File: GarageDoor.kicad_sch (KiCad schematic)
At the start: 30 parts, among them J1 1935161.0, J2 EB21A-04-C, J3 EB21A-04-C, K1 SRD-12VDC-SL-C, K2 SRD-12VDC-SL-C, Q1 BS170-D26Z, Q2 BS170-D26Z, Q3 IRFR9024NTRLPBF, U1 LM2596, U2 WeMos_D1_mini

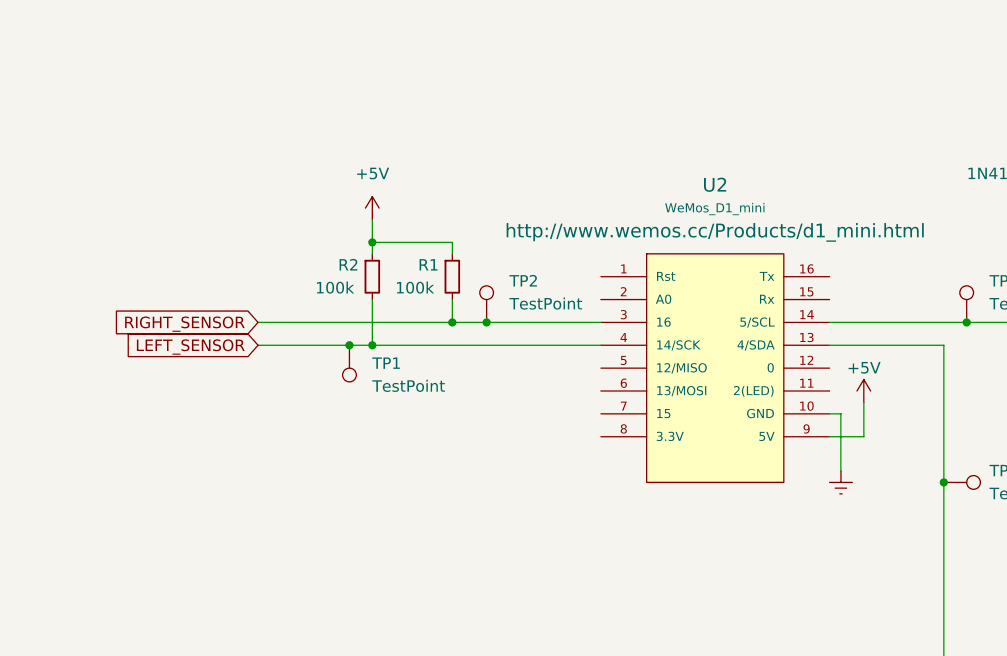
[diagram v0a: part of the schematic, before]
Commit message: Connect unused pins to ground.
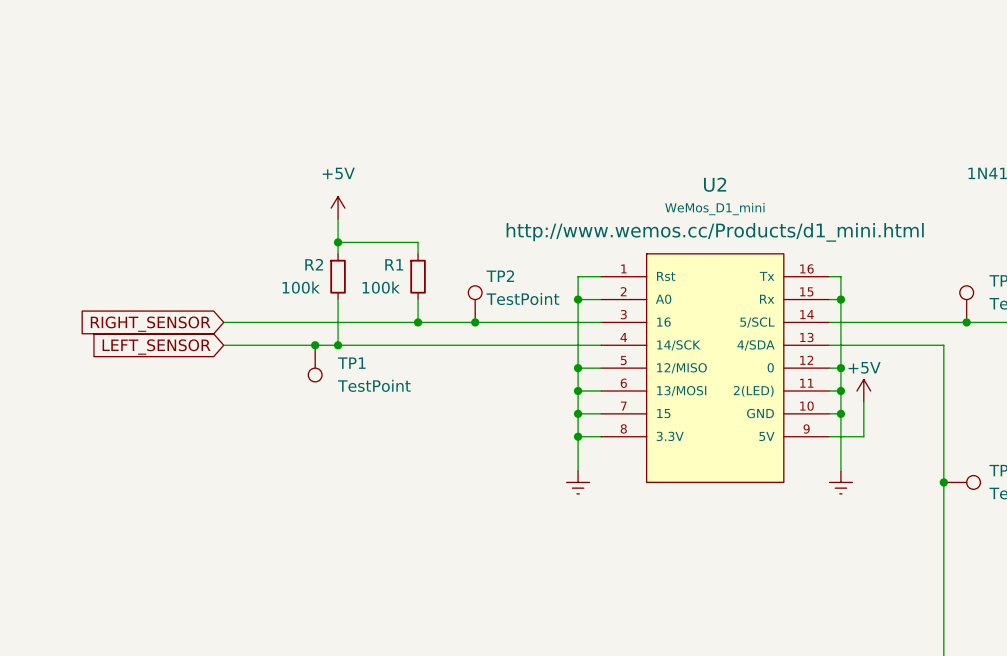
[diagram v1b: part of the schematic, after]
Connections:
- net Earth: now also U2.1 (Rst), U2.11 (2(LED)), U2.12 (0), U2.15 (Rx), U2.16 (Tx), U2.2 (A0), U2.5 (12/MISO), U2.6 (13/MOSI), U2.7 (15), U2.8 (3.3V)
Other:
- moved on the sheet: R1, R2, TP1, TP2

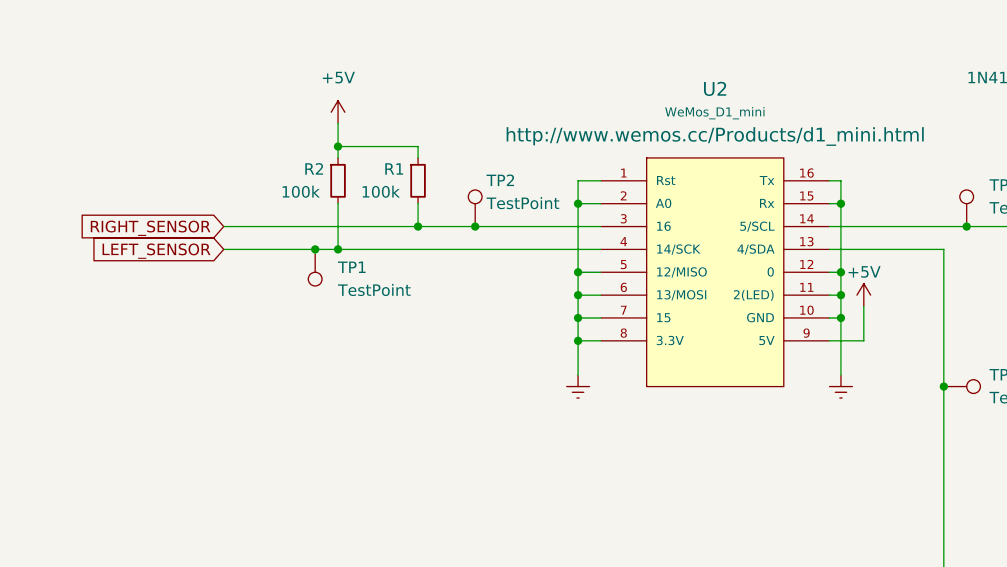
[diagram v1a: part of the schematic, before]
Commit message: Move right sensor to pin 12 instead of 16, because that breaks everything for some reason and you're apparently just supposed to know that.
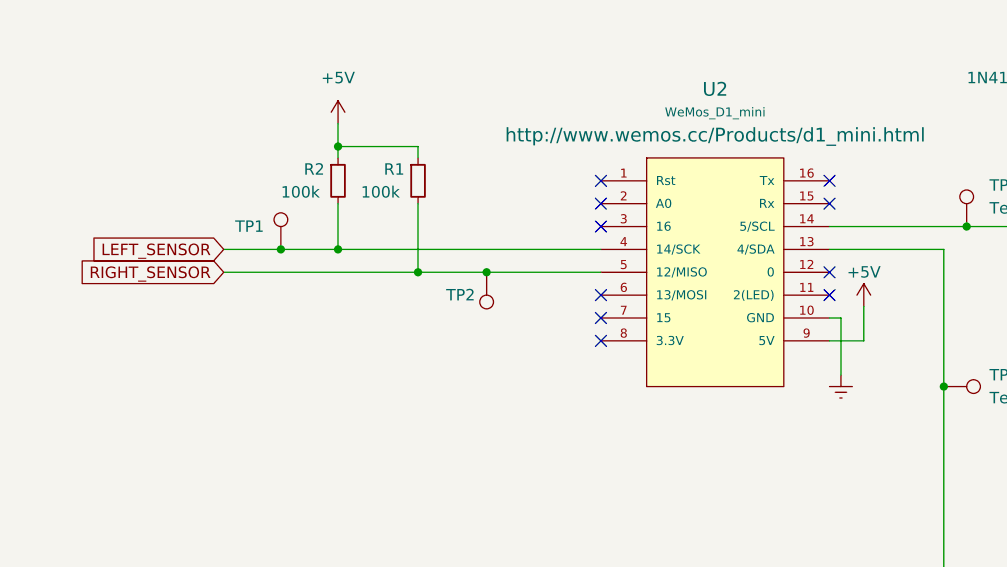
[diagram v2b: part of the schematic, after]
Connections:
- net Earth: no longer U2.1 (Rst), U2.11 (2(LED)), U2.12 (0), U2.15 (Rx), U2.16 (Tx), U2.2 (A0), U2.5 (12/MISO), U2.6 (13/MOSI), U2.7 (15), U2.8 (3.3V)
- net RIGHT_SENSOR: now also U2.5 (12/MISO); no longer U2.3 (16)
- no-connect marks 0 -> 10
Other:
- moved on the sheet: TP1, TP2

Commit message: Add documentation.
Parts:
- J1: Digikey PN 277-1667-ND -> https://www.aliexpress.us/item/3256805408760426.html
- J2, J3: Digikey PN (none) -> https://www.aliexpress.us/item/3256805408760426.html
- JP1: Digikey PN (none) -> S9337-ND
- K1, K2: Digikey PN (none) -> https://www.aliexpress.us/item/3256802839040760.html
- U1: Digikey PN https://a.co/d/2OIi4nQ -> https://www.aliexpress.us/item/3256804718557368.html
- U2: Digikey PN (none) -> https://www.aliexpress.us/item/3256805831695231.html
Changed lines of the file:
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@@
-    (stroke (width 0) (type default))
-  )
-  (polyline (pts (xy 182.88 165.1) (xy 182.88 87.63))
     (stroke (width 0) (type default))
   )
@@
     (stroke (width 0) (type default))
   )
-  (polyline (pts (xy 12.7 160.02) (xy 109.22 160.02))
-    (stroke (width 0) (type default))
-  )
   (wire (pts (xy 226.06 147.32) (xy 226.06 148.59))
     (stroke (width 0) (type default))
@@
     (stroke (width 0) (type default))
   )
-  (polyline (pts (xy 109.22 160.02) (xy 109.22 198.12))
-    (stroke (width 0) (type default))
-  )
   (wire (pts (xy 213.36 130.81) (xy 215.9 130.81))
     (stroke (width 0) (type default))
@@
     (stroke (width 0) (type default))
   )
-  (polyline (pts (xy 284.48 87.63) (xy 182.88 87.63))
-    (stroke (width 0) (type default))
+  (rectangle (start 184.15 86.36) (end 284.48 165.1)
+    (stroke (width 0) (type default))
+    (fill (type none))
+  )
+  (rectangle (start 12.7 152.4) (end 101.6 196.85)
+    (stroke (width 0) (type default))
+    (fill (type none))
   )
   (text "Connectors" (at 234.95 91.44 0)
     (effects (font (size 1.27 1.27)) (justify left bottom))
   )
-  (text "Power" (at 55.88 162.56 0)
+  (text "Power" (at 49.53 156.21 0)
     (effects (font (size 1.27 1.27)) (justify left bottom))
   )
@@
       (effects (font (size 1.27 1.27)) hide)
     )
-    (property "Digikey PN" "277-1667-ND" (at 207.01 152.4 0)
+    (property "Digikey PN" "https://www.aliexpress.us/item/3256805408760426.html" (at 207.01 152.4 0)
       (effects (font (size 1.27 1.27)) hide)
     )
@@
     (property "Datasheet" "http://www.wemos.cc/Products/d1_mini.html" (at 90.17 53.34 0)
       (effects (font (size 1.524 1.524)))
+    )
+    (property "Digikey PN" "https://www.aliexpress.us/item/3256805831695231.html" (at 90.17 67.31 0)
+      (effects (font (size 1.27 1.27)) hide)
     )
     (pin "11")
@@
       (effects (font (size 1.27 1.27)) hide)
     )
+    (property "Digikey PN" "S9337-ND" (at 78.74 176.53 0)
+      (effects (font (size 1.27 1.27)) hide)
+    )
     (pin "2")
     (pin "1")
@@
       (effects (font (size 1.27 1.27)) hide)
     )
+    (property "Digikey PN" "https://www.aliexpress.us/item/3256802839040760.html" (at 146.05 45.72 0)
+      (effects (font (size 1.27 1.27)) hide)
+    )
     (pin "3")
     (pin "5")
@@
       (effects (font (size 1.27 1.27)) hide)
     )
+    (property "Digikey PN" "https://www.aliexpress.us/item/3256802839040760.html" (at 146.05 101.6 0)
+      (effects (font (size 1.27 1.27)) hide)
+    )
     (pin "3")
     (pin "5")
@@
     )
     (property "Datasheet" "~" (at 273.05 152.4 0)
+      (effects (font (size 1.27 1.27)) hide)
+    )
+    (property "Digikey PN" "https://www.aliexpress.us/item/3256805408760426.html" (at 273.05 152.4 0)
       (effects (font (size 1.27 1.27)) hide)
     )
@@
       (effects (font (size 1.27 1.27)) hide)
     )
-    (property "Digikey PN" "https://a.co/d/2OIi4nQ" (at 68.58 184.785 0)
+    (property "Digikey PN" "https://www.aliexpress.us/item/3256804718557368.html" (at 68.58 184.785 0)
       (effects (font (size 1.27 1.27)) hide)
     )
@@
       (effects (font (size 1.27 1.27)) hide)
     )
+    (property "Digikey PN" "https://www.aliexpress.us/item/3256805408760426.html" (at 242.57 152.4 0)
+      (effects (font (size 1.27 1.27)) hide)
+    )
